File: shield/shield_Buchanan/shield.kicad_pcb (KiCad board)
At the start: 2 copper layers, 27 parts, among them CN10 Conn_02x17_Odd_Even, CN7 Conn_02x10_Odd_Even, CN8 Conn_02x08_Odd_Even, CN9 Conn_02x15_Odd_Even, J1 Screw_Terminal_01x04, J10 Screw_Terminal_01x04, J11 Screw_Terminal_01x04, J12 Screw_Terminal_01x04, J2 Screw_Terminal_01x04, J3 Screw_Terminal_01x04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

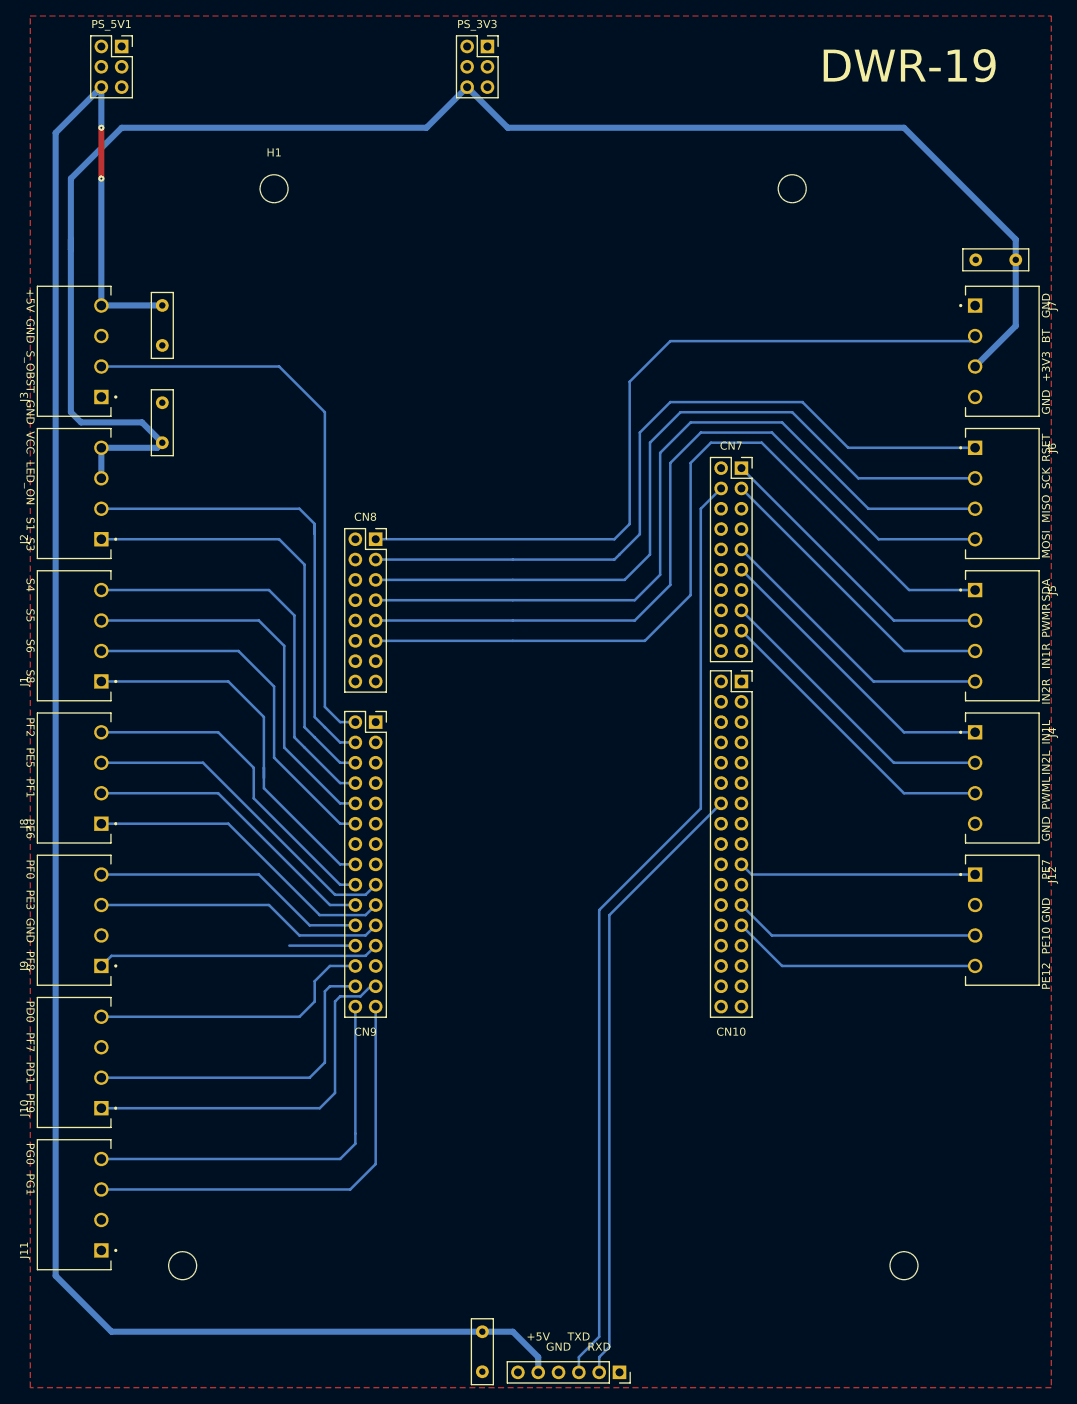
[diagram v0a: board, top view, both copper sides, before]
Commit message: Update PCB with new pins -> ADC3
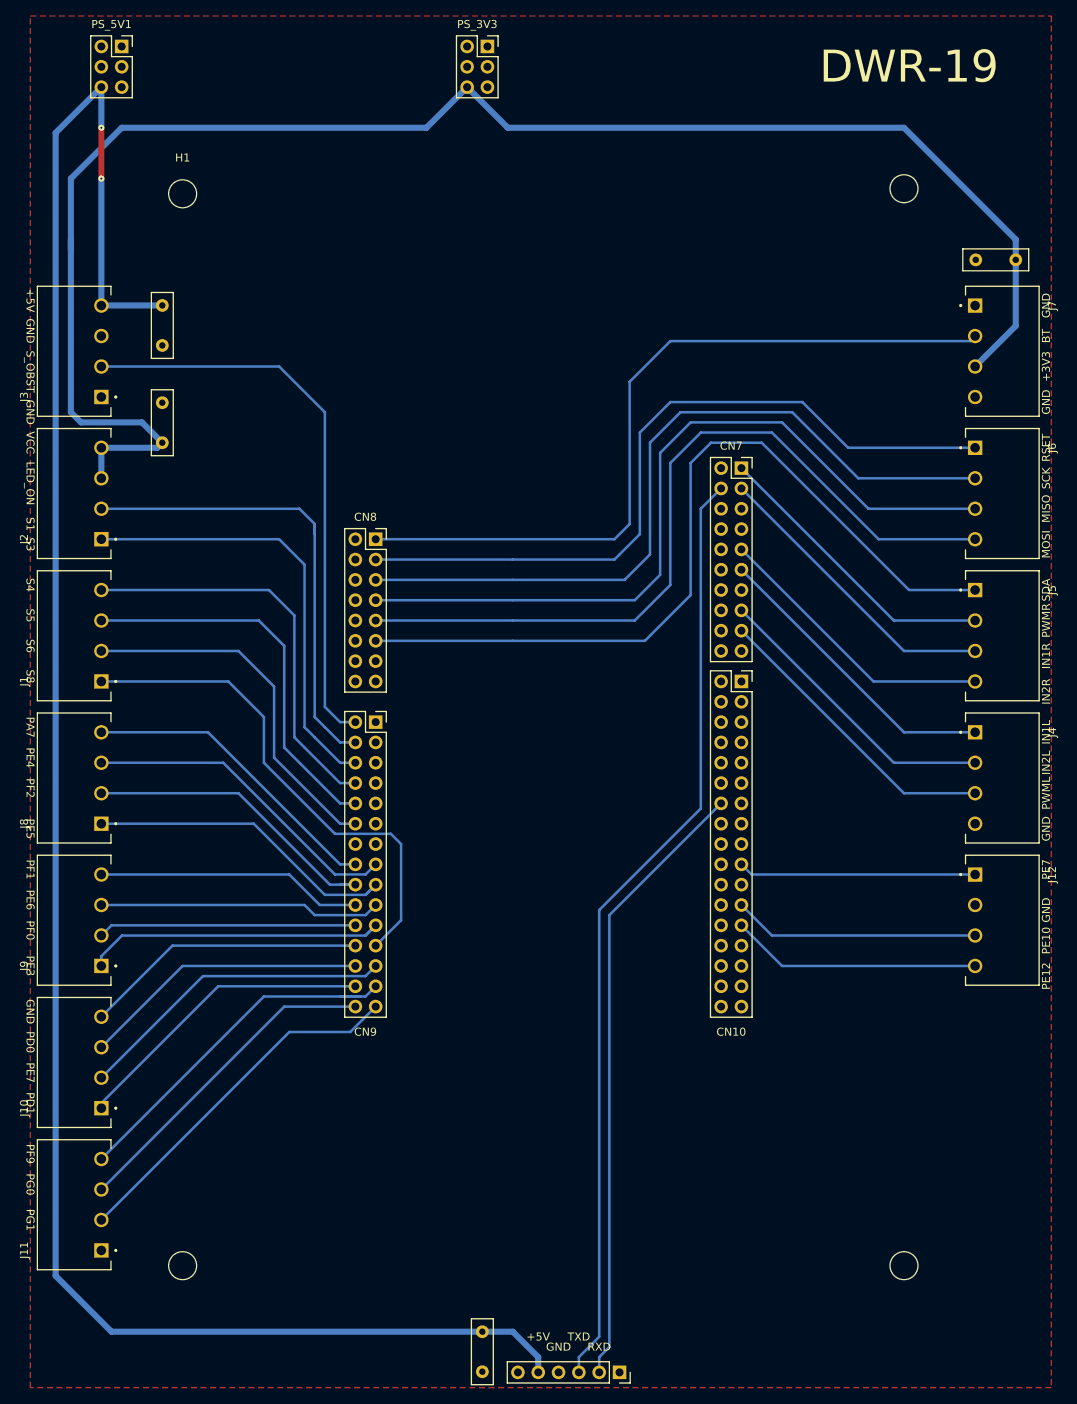
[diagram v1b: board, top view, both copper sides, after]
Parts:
- moved H3 14.0 mm to (148.6, 45.7)
- moved H1 11.4 mm to (58.4, 46.4)
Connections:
- CN9 pad 25: PF7´ -> PF7
- J1 pad 1: PA7 -> PF8
- J10 pad 1: PF9 -> PD1
- J10 pad 2: PD1 -> PF7
- J10 pad 3: PF7 -> PD0
- J10 pad 4: PD0 -> GND
- J11 pad 2: Net-(J11-Pad2) -> PG1
- J11 pad 3: PG1 -> PG0
- J11 pad 4: PG0 -> PF9
- J8 pad 1: PE6 -> PE5
- J8 pad 2: PF1 -> PF2
- J8 pad 3: PE5 -> PE4
- J8 pad 4: PF2 -> PA7
- J9 pad 1: PF8 -> PE3
- J9 pad 2: GND -> PF0
- J9 pad 3: PE3 -> PE6
- J9 pad 4: PF0 -> PF1
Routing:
- net PE4: track 0.00 -> 41.2 mm
- net PF7: track 0.00 -> 40.1 mm
- net PF8: track 36.0 -> 63.9 mm
- net GND: track 8.89 -> 36.1 mm
- net PG1: track 55.3 -> 45.3 mm
- net PA7: track 47.7 -> 38.6 mm
- net PG0: track 49.7 -> 41.2 mm
- net PE6: track 39.5 -> 35.3 mm
- net PF1: track 37.5 -> 33.3 mm
- net PF2: track 42.5 -> 39.0 mm
- net PD1: track 41.7 -> 38.4 mm
- net PE3: track 36.4 -> 38.9 mm
- net PF0: track 34.4 -> 32.3 mm
- net PE5: track 42.3 -> 40.3 mm
- net PF9: track 47.3 -> 46.4 mm
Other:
- board text added: "PA7"
- board text added: "PE4"
- board text removed: "PF7"
- board text removed: "PF8"

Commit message: pcb adc 3
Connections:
- J12 pad 1: PE7 -> PB1
- J12 pad 2: GND -> PC2
- J12 pad 3: PE10 -> PF4
- J12 pad 4: PE12 -> PA0
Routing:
- net PF4: track 0.00 -> 39.6 mm
- net PC2: track 0.00 -> 39.1 mm
- net PB1: track 0.00 -> 38.6 mm
- net PA0: track 0.00 -> 32.8 mm
- net PE12: track 31.3 -> 0.00 mm
- net PE10: track 30.8 -> 0.00 mm
- net PE7: track 29.7 -> 0.00 mm
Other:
- board text added: "PA0"
- board text added: "PB1"
- board text added: "PC2"
- board text added: "PF4"
- board text removed: "PE10"
- board text removed: "PE12"

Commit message: last update Kicad
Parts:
- moved C_SLINHA1 10.2 mm to (66.0, 77.5)
- moved C_SOBST1 10.2 mm to (66.0, 60.3)
- moved J1 10.2 mm to (58.4, 101.6)
- moved J10 10.2 mm to (58.4, 154.9)
- moved J11 10.2 mm to (58.4, 172.7)
- moved J2 10.2 mm to (58.4, 83.8)
- moved J3 10.2 mm to (58.4, 66.0)
- moved J8 10.2 mm to (58.4, 119.4)
- moved J9 10.2 mm to (58.4, 137.2)
- moved C_RFID1 10.2 mm to (152.4, 54.6)
- moved J12 10.2 mm to (147.3, 137.2)
- moved J4 10.2 mm to (147.3, 119.4)
- moved J5 10.2 mm to (147.3, 101.6)
- moved J6 10.2 mm to (147.3, 83.8)
- moved J7 10.2 mm to (147.3, 66.0)
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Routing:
- net GND: track 36.1 -> 0.64 mm
- net +5V: track 253.0 -> 267.7 mm
- net +3V3: track 203.9 -> 189.5 mm
- net PF9: track 46.4 -> 34.1 mm
- net PE3: track 38.9 -> 28.0 mm
- net PE4: track 41.2 -> 30.4 mm
- net PD1: track 38.4 -> 27.9 mm
- net PF5: track 48.7 -> 38.5 mm
- net PF3: track 50.7 -> 40.5 mm
- net PA3: track 71.7 -> 61.6 mm
- net PF8: track 63.9 -> 53.7 mm
- net PF10: track 45.9 -> 35.7 mm
- net PF1: track 33.3 -> 23.2 mm
- net PF0: track 32.3 -> 22.1 mm
- net PE5: track 40.3 -> 30.1 mm
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- added copper zone on B.Cu, net GND
- removed copper zone on F.Cu, net GND

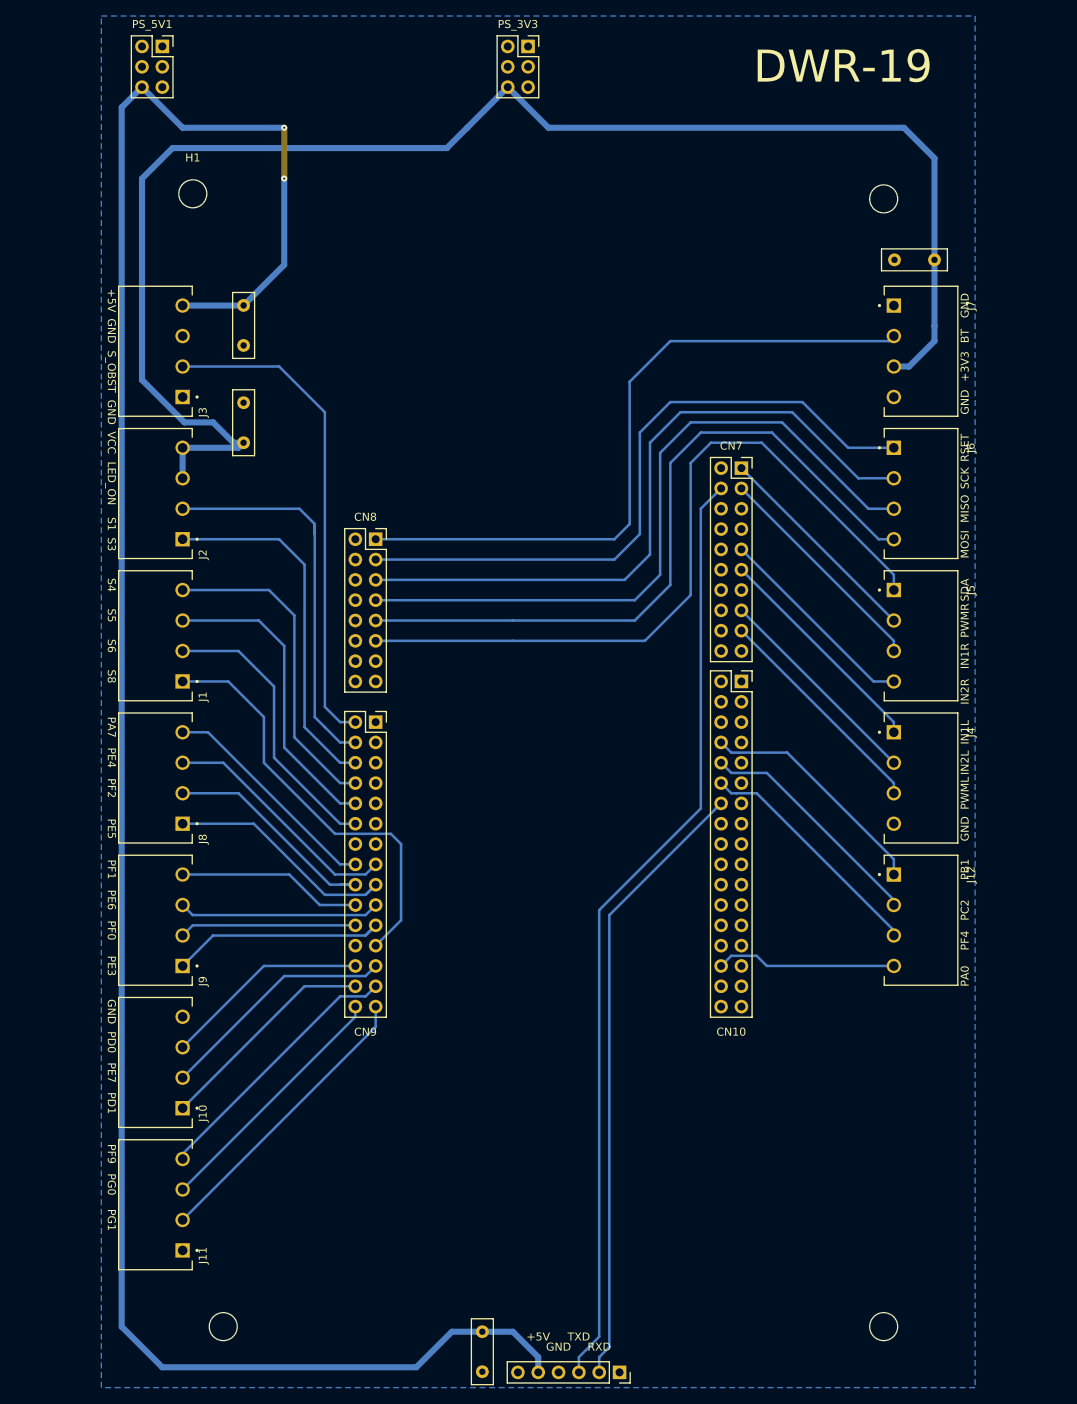
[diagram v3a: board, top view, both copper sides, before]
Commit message: Buracos 4mm
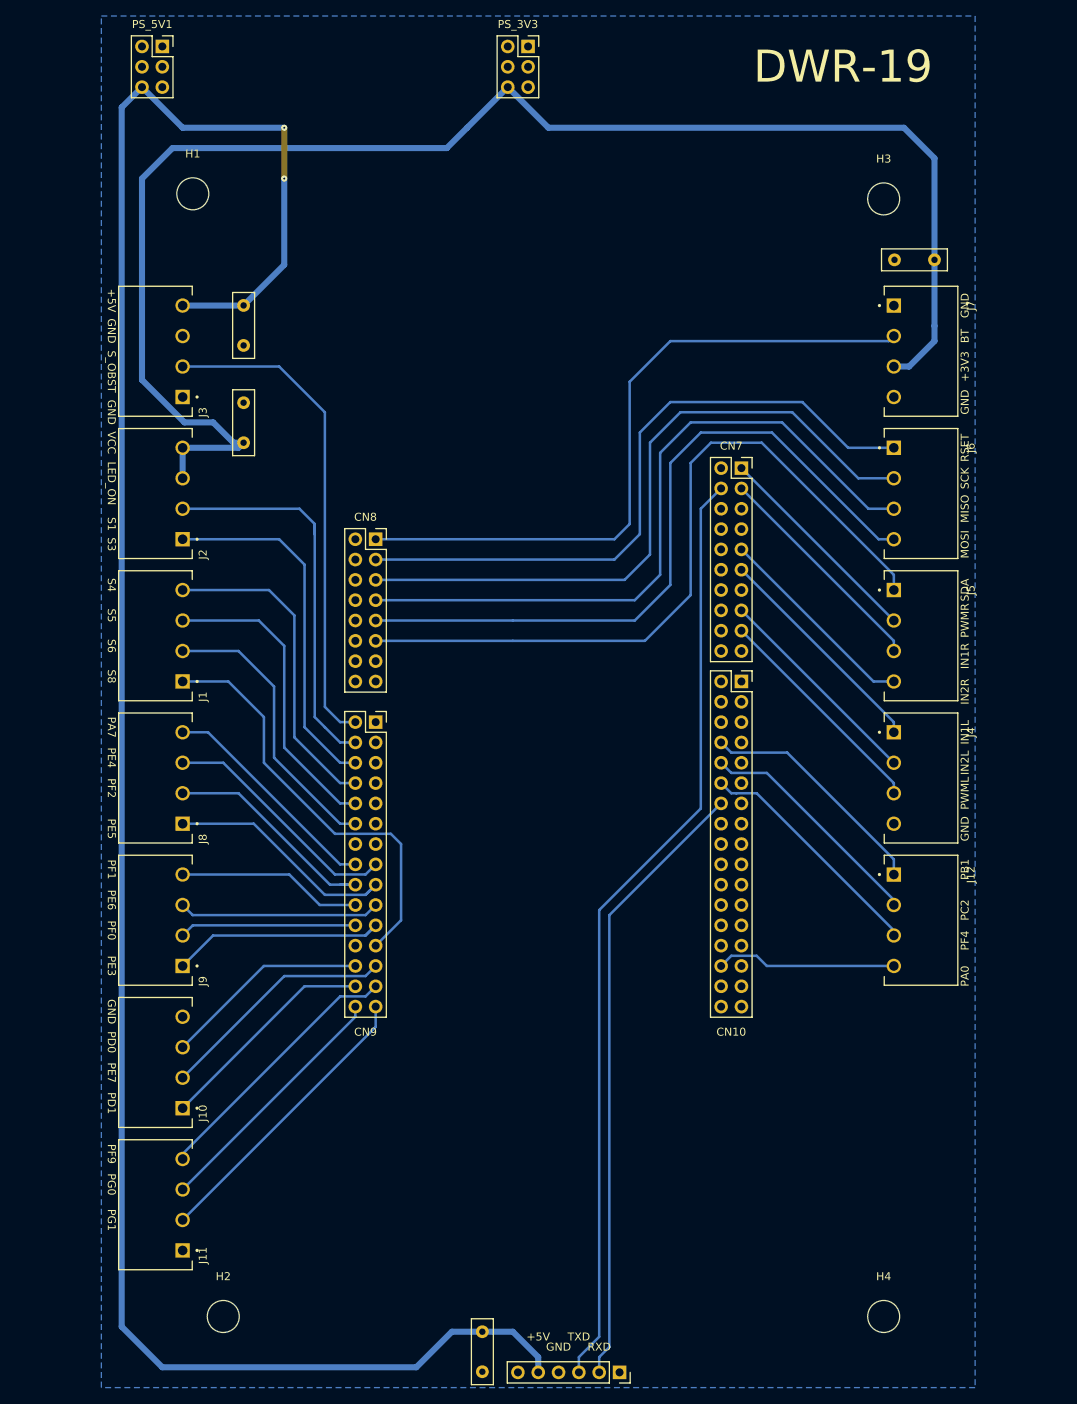
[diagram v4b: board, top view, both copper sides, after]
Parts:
- H1, H2, H3, H4: footprint MountingHole:MountingHole_3.5mm -> MountingHole:MountingHole_4mm
- moved H2 1.27 mm to (63.5, 186.7)
- moved H4 1.27 mm to (146.1, 186.7)
